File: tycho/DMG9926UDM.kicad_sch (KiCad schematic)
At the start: 3 parts

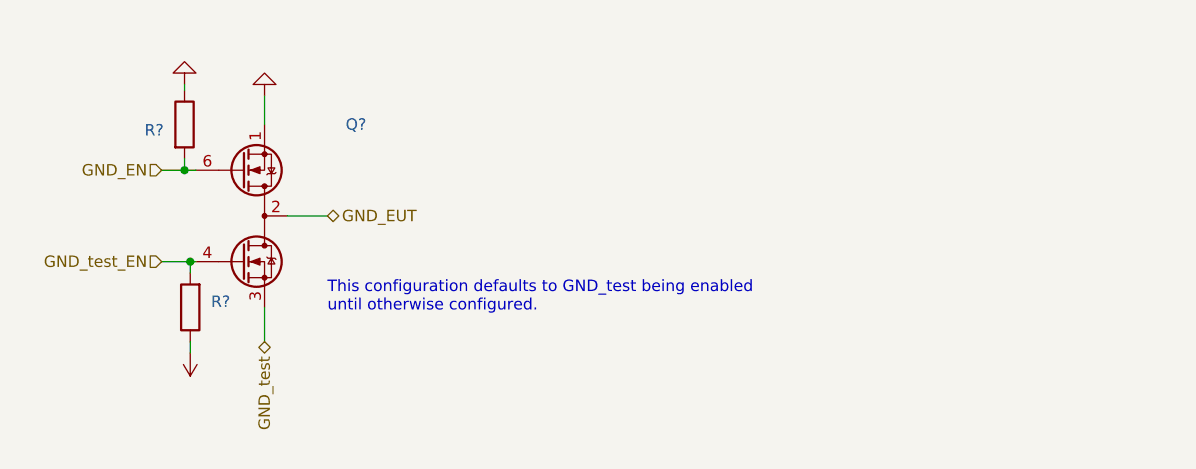
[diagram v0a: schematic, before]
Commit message: Tycho Hardware: Reduce D+- switches to 4 and re-route
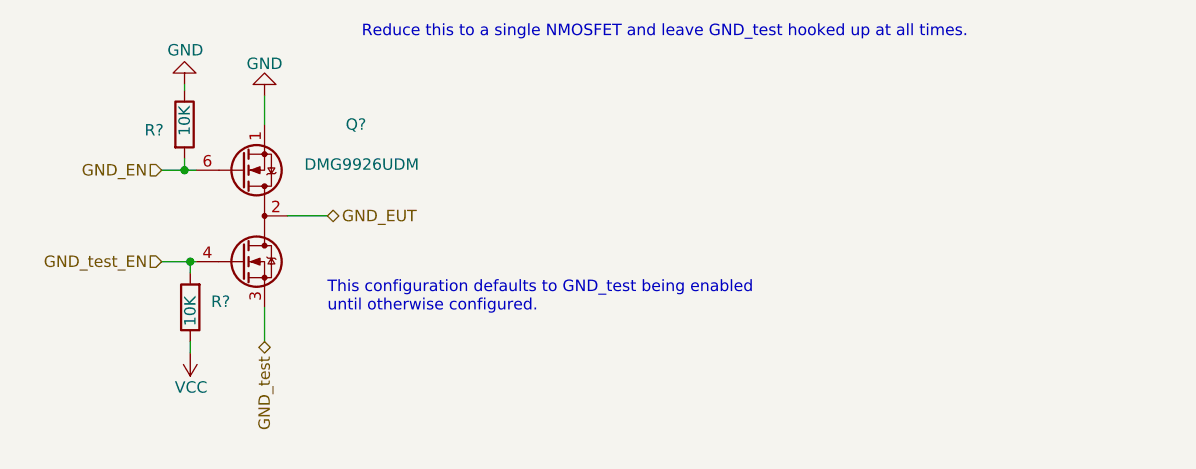
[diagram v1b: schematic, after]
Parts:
- Q?: value (none) -> DMG9926UDM; footprint (none) -> Package_TO_SOT_SMD:SOT-23-6
- R? (x2): value (none) -> 10K; footprint (none) -> Resistor_SMD:R_0603_1608Metric_Pad0.98x0.95mm_HandSolder
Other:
- note added: "Reduce this to a single NMOSFET and leave GND_test hooked up at all times."
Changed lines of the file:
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@@
+    (effects (font (size 1.27 1.27)) (justify left bottom))
+  )
+  (text "Reduce this to a single NMOSFET and leave GND_test hooked up at all times."
+    (at 167.005 55.88 0)
     (effects (font (size 1.27 1.27)) (justify left bottom))
   )
@@
       (effects (font (size 1.27 1.27)) (justify left))
     )
-    (property "Value" "" (id 1) (at 147.955 84.455 90)
+    (property "Value" "10K" (id 1) (at 147.955 84.455 90)
       (effects (font (size 1.27 1.27)) (justify left))
     )
-    (property "Footprint" "" (id 2) (at 149.733 85.725 90)
+    (property "Footprint" "Resistor_SMD:R_0603_1608Metric_Pad0.98x0.95mm_HandSolder" (id 2) (at 149.733 85.725 90)
       (effects (font (size 1.27 1.27)) hide)
     )
@@
     (in_bom yes) (on_board yes)
     (property "Reference" "Q?" (id 0) (at 166.37 65.405 0))
-    (property "Value" "" (id 1) (at 167.005 69.85 0))
-    (property "Footprint" "" (id 2) (at 158.75 68.58 0)
+    (property "Value" "DMG9926UDM" (id 1) (at 167.005 69.85 0))
+    (property "Footprint" "Package_TO_SOT_SMD:SOT-23-6" (id 2) (at 158.75 68.58 0)
       (effects (font (size 1.27 1.27) italic) (justify left) hide)
     )
@@
       (effects (font (size 1.27 1.27)) hide)
     )
-    (property "Value" "" (id 1) (at 145.415 57.15 0)
+    (property "Value" "GND" (id 1) (at 145.415 57.15 0)
       (effects (font (size 1.27 1.27)) (justify right))
     )
@@
       (effects (font (size 1.27 1.27)) (justify left))
     )
-    (property "Value" "" (id 1) (at 147.32 66.675 90)
+    (property "Value" "10K" (id 1) (at 147.32 66.675 90)
       (effects (font (size 1.27 1.27)) (justify left))
     )
-    (property "Footprint" "" (id 2) (at 145.542 65.405 90)
+    (property "Footprint" "Resistor_SMD:R_0603_1608Metric_Pad0.98x0.95mm_HandSolder" (id 2) (at 145.542 65.405 90)
       (effects (font (size 1.27 1.27)) hide)
     )
@@
       (effects (font (size 1.27 1.27)) hide)
     )
-    (property "Value" "" (id 1) (at 149.86 94.615 0)
+    (property "Value" "VCC" (id 1) (at 149.86 94.615 0)
       (effects (font (size 1.27 1.27)) (justify left))
     )
@@
       (effects (font (size 1.27 1.27)) hide)
     )
-    (property "Value" "" (id 1) (at 156.21 58.6542 0))
+    (property "Value" "GND" (id 1) (at 156.21 58.6542 0))
     (property "Footprint" "" (id 2) (at 156.21 62.23 0)
       (effects (font (size 1.27 1.27)) hide)
